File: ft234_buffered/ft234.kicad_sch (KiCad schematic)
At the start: 16 parts, among them J1 USB_OTG, J2 Conn_01x04, U1 FT234XD, U2 74LVC1G17, U3 74LVC1G17

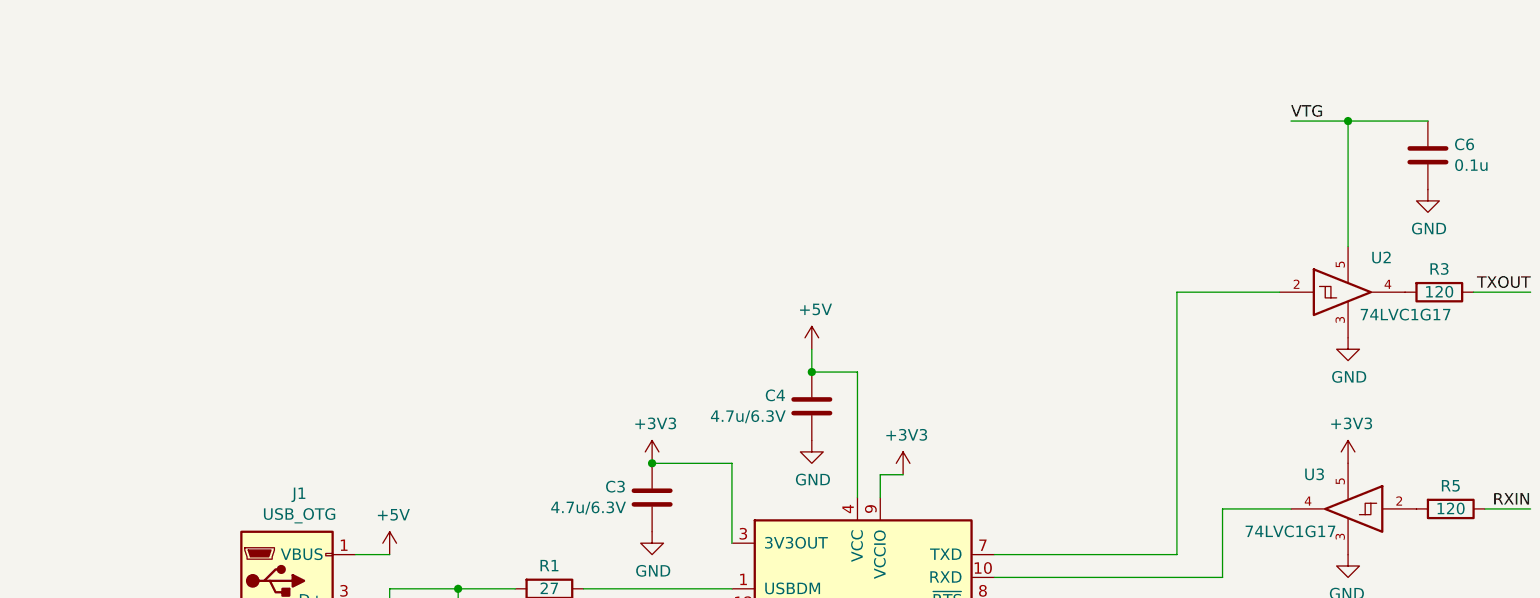
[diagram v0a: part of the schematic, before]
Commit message: changing buffered ft234 board - wip
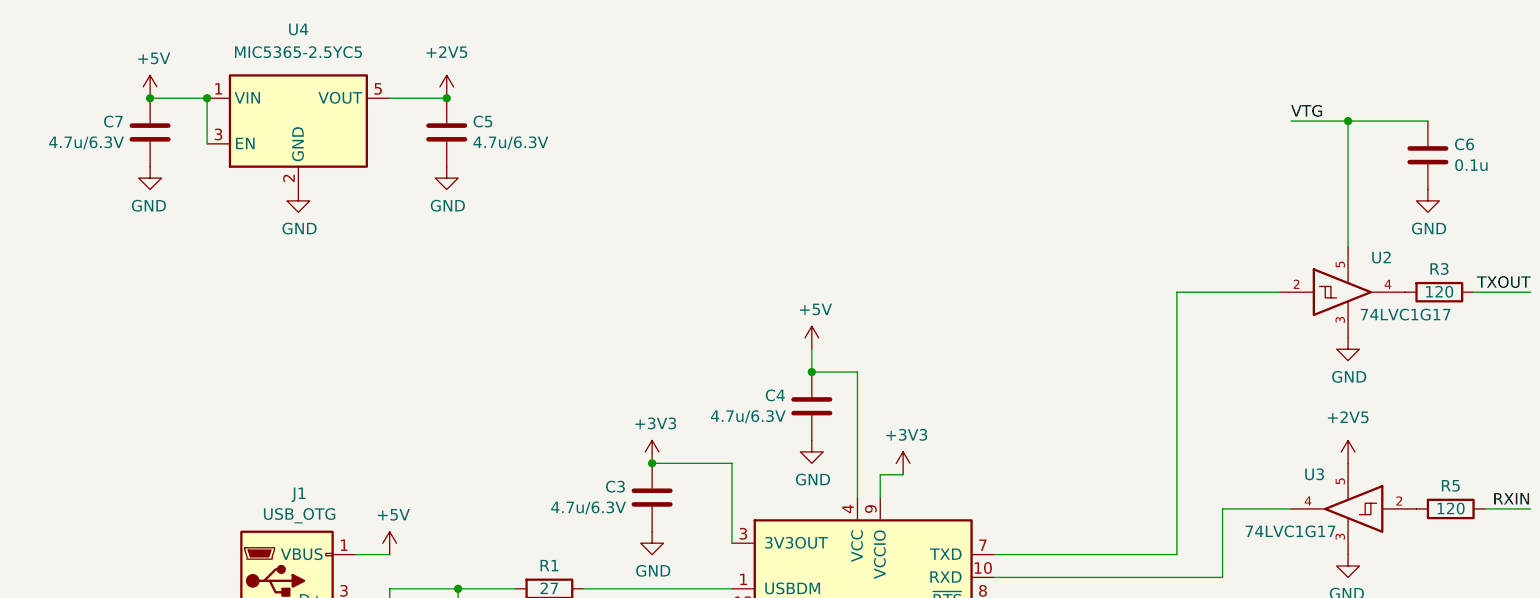
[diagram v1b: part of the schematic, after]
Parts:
- added C5, C7: 4.7u/6.3V, Capacitor_SMD:C_0603_1608Metric, symbol Device:C
- added U4: MIC5365-2.5YC5, Package_TO_SOT_SMD:SOT-353_SC-70-5, symbol Regulator_Linear:MIC5365-3.3YC5
- C1, C2: footprint Capacitors_SMD:C_0402_NoSilk -> Capacitor_SMD:C_0402_1005Metric
- C3, C4: footprint Capacitors_SMD:C_0603 -> Capacitor_SMD:C_0603_1608Metric
- D1: footprint LEDs:LED_0603 -> LED_SMD:LED_0603_1608Metric
- J1: footprint hunz:USB_Micro-B_10103594-0001LF -> Connector_USB:USB_Micro-B_Amphenol_10103594-0001LF_Horizontal
- R1, R2, R3, R4, R5: footprint Resistors_SMD:R_0402_NoSilk -> Resistor_SMD:R_0402_1005Metric
- U1: footprint Housings_DFN_QFN:DFN-12-1EP_3x3mm_Pitch0.45mm -> Package_DFN_QFN:DFN-12-1EP_3x3mm_P0.45mm_EP1.66x2.38mm
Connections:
- net +3V3: no longer U3.5
- net +5V: now also C7.1, U4.1 (VIN), U4.3 (EN)
- net GND: now also C5.2, C7.2, U4.2 (GND)
- new net +2V5: C5.1, U3.5, U4.5 (VOUT)

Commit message: wip
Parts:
- C3, C4, C5, C7: footprint Capacitor_SMD:C_0603_1608Metric -> Capacitor_SMD:C_0402_1005Metric
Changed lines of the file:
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@@
       (effects (font (size 1.27 1.27)) (justify left))
     )
-    (property "Footprint" "Capacitor_SMD:C_0603_1608Metric" (at 113.3348 83.82 0)
+    (property "Footprint" "Capacitor_SMD:C_0402_1005Metric" (at 113.3348 83.82 0)
       (effects (font (size 1.27 1.27)) hide)
     )
@@
       (effects (font (size 1.27 1.27)) (justify left))
     )
-    (property "Footprint" "Capacitor_SMD:C_0603_1608Metric" (at 131.1148 73.66 0)
+    (property "Footprint" "Capacitor_SMD:C_0402_1005Metric" (at 131.1148 73.66 0)
       (effects (font (size 1.27 1.27)) hide)
     )
@@
       (effects (font (size 1.27 1.27)) (justify left))
     )
-    (property "Footprint" "Capacitor_SMD:C_0603_1608Metric" (at 57.4548 43.18 0)
+    (property "Footprint" "Capacitor_SMD:C_0402_1005Metric" (at 57.4548 43.18 0)
       (effects (font (size 1.27 1.27)) hide)
     )
@@
       (effects (font (size 1.27 1.27)) (justify left))
     )
-    (property "Footprint" "Capacitor_SMD:C_0603_1608Metric" (at 92.4052 43.18 0)
-      (effects (font (size 1.27 1.27)) hide)
-    )
+    (property "Footprint" "Capacitor_SMD:C_0402_1005Metric" (at 92.4052 43.18 0)
+      (effects (font (size 1.27 1.27)) hide)
+    )

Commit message: done
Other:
- note added: "74LVC1G17: @Vdd=2.5V: positive-going threshold: <=1.5V FT234 VddIO: 3.3V - positive-going threshold: <= 2.0V"
- note added: "74LVC1G17: @Vdd=5V: positive-going threshold: <=2.6V FT234 VddIO: 3.3V"
- note added: "Vtarget range: 1.8V .. ~5.0V"
- moved on the sheet: C1, C2, C3, C4, C5, C6, C7, D1, J1, J2, R1, R2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

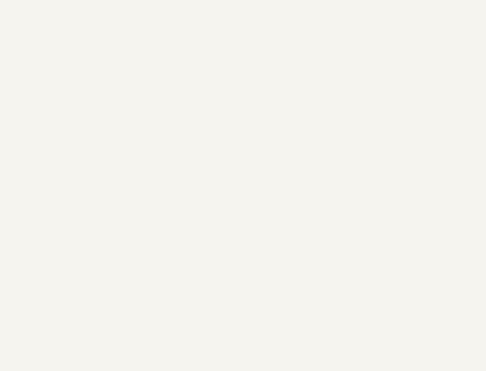
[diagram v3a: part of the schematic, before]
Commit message: add fiducials
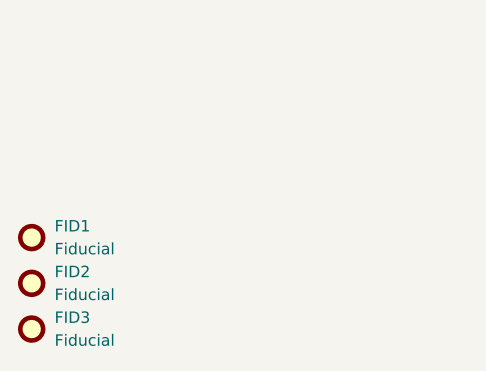
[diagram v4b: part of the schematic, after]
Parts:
- added FID1, FID2, FID3: Fiducial, Fiducial:Fiducial_0.5mm_Mask1mm, symbol Mechanical:Fiducial
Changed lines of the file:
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@@
+    )
+  )
+  (symbol (lib_id "Mechanical:Fiducial") (at 36.83 173.99 0) (unit 1)
+    (in_bom yes) (on_board yes) (dnp no) (fields_autoplaced)
+    (property "Reference" "FID1" (at 39.37 172.72 0)
+      (effects (font (size 1.27 1.27)) (justify left))
+    )
+    (property "Value" "Fiducial" (at 39.37 175.26 0)
+      (effects (font (size 1.27 1.27)) (justify left))
+    )
+    (property "Footprint" "Fiducial:Fiducial_0.5mm_Mask1mm" (at 36.83 173.99 0)
+      (effects (font (size 1.27 1.27)) hide)
+    )
+    (property "Datasheet" "~" (at 36.83 173.99 0)
+      (effects (font (size 1.27 1.27)) hide)
+    )
+    (instances
+      (project "ft234"
+        (path "/1f08e041-63eb-4c92-ae2b-bdba754c2965"
+          (reference "FID1") (unit 1)
+        )
+      )
     )
   )
@@
         (path "/1f08e041-63eb-4c92-ae2b-bdba754c2965"
           (reference "#PWR018") (unit 1)
+        )
+      )
+    )
+  )
+  (symbol (lib_id "Mechanical:Fiducial") (at 36.83 184.15 0) (unit 1)
+    (in_bom yes) (on_board yes) (dnp no) (fields_autoplaced)
+    (property "Reference" "FID3" (at 39.37 182.88 0)
+      (effects (font (size 1.27 1.27)) (justify left))
+    )
+    (property "Value" "Fiducial" (at 39.37 185.42 0)
+      (effects (font (size 1.27 1.27)) (justify left))
+    )
+    (property "Footprint" "Fiducial:Fiducial_0.5mm_Mask1mm" (at 36.83 184.15 0)
+      (effects (font (size 1.27 1.27)) hide)
+    )
+    (property "Datasheet" "~" (at 36.83 184.15 0)
+      (effects (font (size 1.27 1.27)) hide)
+    )
+    (instances
+      (project "ft234"
+        (path "/1f08e041-63eb-4c92-ae2b-bdba754c2965"
+          (reference "FID3") (unit 1)
         )
       )
@@
         )
       )
+    )
+  )
+  (symbol (lib_id "Mechanical:Fiducial") (at 36.83 179.07 0) (unit 1)
+    (in_bom yes) (on_board yes) (dnp no) (fields_autoplaced)
+    (property "Reference" "FID2" (at 39.37 177.8 0)
+      (effects (font (size 1.27 1.27)) (justify left))
+    )
+    (property "Value" "Fiducial" (at 39.37 180.34 0)
+      (effects (font (size 1.27 1.27)) (justify left))
+    )
+    (property "Footprint" "Fiducial:Fiducial_0.5mm_Mask1mm" (at 36.83 179.07 0)
+      (effects (font (size 1.27 1.27)) hide)
+    )
+    (property "Datasheet" "~" (at 36.83 179.07 0)
+      (effects (font (size 1.27 1.27)) hide)
+    )
+    (instances
+      (project "ft234"
+        (path "/1f08e041-63eb-4c92-ae2b-bdba754c2965"
+          (reference "FID2") (unit 1)
+        )
+      )
